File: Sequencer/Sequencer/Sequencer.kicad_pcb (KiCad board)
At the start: 2 copper layers, 163 x 116.5 mm, 158 parts, among them J1 Conn_02x05_Odd_Even, J10 Conn_01x08, J11 Conn_01x08, J12 Conn_01x08, J2 Conn_01x08, J3 Conn_01x08, J4 Conn_01x03, J5 Conn_01x04, J6 Conn_01x05, J7 Conn_01x04, J8 Conn_01x08, J9 Conn_01x08, Q1 2N3904, U1 4013, U10 TL074, U11 TL072, U12 LM285Z-ADJ, U2 40106, U3 40106, U4 40193, U5 40106, U6 4514, U7 TL072, U8 CD4094, U9 CD74HC4067M

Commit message: Sequencer - minor progress on routing
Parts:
- C1, C11, C12, C13, C14, C15, C16, C17, C2, C20, C21, C22, C23, C24, C25, C26, C27, C3, C4, C5, C6, C7, C8, C9: footprint Capacitor_THT:C_Disc_D3.0mm_W1.6mm_P2.50mm -> Capacitor_THT:C_Disc_D5.0mm_W2.5mm_P2.50mm
- R1, R10, R11, R12, R13, R14, R15, R16, R17, R18, R19, R2, R20, R21, R22, R23, R24, R25, R26, R27, R28, R29, R3, R30, R31, R32, R33, R34, R35, R36, R37, R38, R39, R4, R40, R41, R42, R43, R44, R45, R46, R47, R48, R49, R5, R50, R51, R52, R53, R54, R55, R56, R57, R58, R59, R6, R60, R61, R62, R63, R64, R65, R66, R67, R68, R69, R7, R70, R71, R72, R73, R74, R75, R76, R77, R78, R79, R8, R80, R81, R82, R83, R84, R85, R86, R87, R9: footprint Resistor_THT:R_Axial_DIN0207_L6.3mm_D2.5mm_P7.62mm_Horizontal -> Library:R_Axial_DIN0207_L6.3mm_D2.5mm_P7.62mm_Horizontal
- U6, U9: footprint Package_SO:SOIC-24W_7.5x15.4mm_P1.27mm -> Package_DIP:DIP-24_W15.24mm_Socket_LongPads
- moved R50 294.4 mm to (4.57, 29.5), turned to 90 degrees
- moved R49 290.4 mm to (7.11, 29.5), turned to 90 degrees
- moved R56 271.9 mm to (26.4, 21.6), turned to 90 degrees
- moved R48 269.2 mm to (9.65, 21.6), turned to 90 degrees
- moved R52 268.4 mm to (14.7, 21.6), turned to 90 degrees
- moved R55 267.7 mm to (29.0, 21.6), turned to 90 degrees
- moved R47 265.4 mm to (12.2, 21.6), turned to 90 degrees
- moved R51 264.5 mm to (17.3, 21.6), turned to 90 degrees
- moved R58 260.8 mm to (31.5, 21.6), turned to 90 degrees
- moved R62 260.0 mm to (41.7, 21.6), turned to 90 degrees
- moved R57 256.9 mm to (34.0, 21.6), turned to 90 degrees
- moved R54 256.1 mm to (19.8, 21.6), turned to 90 degrees
- moved R61 255.9 mm to (44.2, 21.6), turned to 90 degrees
- moved R53 252.4 mm to (22.4, 21.6), turned to 90 degrees
- moved C27 247.4 mm to (17.8, 34.5), turned to 180 degrees
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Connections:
- C1 pad 1: STRN -> Net-(C1-Pad1)
- C26 pad 2: Net-(U10C-+) -> PORT_3
- C3 pad 1: STRN -> Net-(C1-Pad1)
- D14 pad 1: GND -> DN
- D15 pad 1: GND -> UP
- J2 pad 1: S1 -> FWD
- J6 pad 2: unconnected-(J6-Pin_2-Pad2) -> CLKOUT
- R1 pad 1: STRN -> Net-(C1-Pad1)
- R1 pad 2: Net-(R1-Pad2) -> STRN
- R3 pad 2: STRN -> Net-(C1-Pad1)
- R41 pad 1: unconnected-(R41-Pad1) -> Net-(R41-Pad1)
- R42 pad 2: Net-(R42-Pad2) -> Net-(R41-Pad1)
- R43 pad 2: Net-(R42-Pad2) -> Net-(R41-Pad1)
- R47 pad 1: F2 -> FR2
- R48 pad 1: F2 -> FR2
- R49 pad 1: F1 -> FR1
- R50 pad 1: F1 -> FR1
- R51 pad 1: F3 -> FR3
- R52 pad 1: F3 -> FR3
- R53 pad 1: F4 -> FR4
- R54 pad 1: F4 -> FR4
- R55 pad 1: F5 -> FR5
- R56 pad 1: F5 -> FR5
- R57 pad 1: F6 -> FR6
- R58 pad 1: F6 -> FR6
- R59 pad 1: F7 -> FR7
- R60 pad 1: F7 -> FR7
- R61 pad 1: F8 -> FR8
- R62 pad 1: F8 -> FR8
- R63 pad 1: F9 -> FR9
- R64 pad 1: F9 -> FR9
- R65 pad 1: F10 -> FR10
- R66 pad 1: F10 -> FR10
- R67 pad 1: F11 -> FR11
- R68 pad 1: F11 -> FR11
- R69 pad 1: F12 -> FR12
- R70 pad 1: F12 -> FR12
- R71 pad 1: F13 -> FR13
- R72 pad 1: F13 -> FR13
- R73 pad 1: F14 -> FR14
- R74 pad 1: F14 -> FR14
- R75 pad 1: F15 -> FR15
- R76 pad 1: F15 -> FR15
- R77 pad 1: F16 -> FR16
- R78 pad 1: F16 -> FR16
- R86 pad 1: Net-(U10B-+) -> PORT_1_2
- U10 pad 10: Net-(U10C-+) -> PORT_3
- U10 pad 12: Net-(U10B-+) -> PORT_1_2
- U10 pad 5: Net-(U10B-+) -> PORT_1_2
- U6 pad 11: S1 -> FWD
- U7 pad 1: Net-(R42-Pad2) -> Net-(R41-Pad1)
- U9 pad 16: F1 -> FR16
- U9 pad 17: F1 -> FR15
- U9 pad 18: F1 -> FR14
- U9 pad 19: F1 -> FR13
- U9 pad 2: F1 -> FR8
- U9 pad 20: F1 -> FR12
- U9 pad 21: F1 -> FR11
- U9 pad 22: F1 -> FR10
- U9 pad 23: F1 -> FR9
- U9 pad 3: F1 -> FR7
- U9 pad 4: F1 -> FR6
- U9 pad 5: F1 -> FR5
- U9 pad 6: F1 -> FR4
- U9 pad 7: F1 -> FR3
- U9 pad 8: F1 -> FR2
- U9 pad 9: F1 -> FR1
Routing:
- net FR16: track 0.00 -> 53.2 mm
- net FR1: track 0.00 -> 51.5 mm
- net FR15: track 0.00 -> 46.2 mm
- net FR2: track 0.00 -> 46.1 mm
- net FR14: track 0.00 -> 39.6 mm
- net FR3: track 0.00 -> 38.8 mm
- net Net-(R41-Pad1): track 0.00 -> 35.6 mm
- net FR13: track 0.00 -> 32.0 mm
- net FR4: track 0.00 -> 31.8 mm
- net FR12: track 0.00 -> 23.2 mm
- net FR5: track 0.00 -> 23.0 mm
- net Net-(C27-Pad1): track 0.00 -> 18.3 mm
- net Net-(D5-A): track 0.00 -> 17.0 mm
- net Net-(C5-Pad1): track 0.00 -> 16.4 mm
- net Net-(C4-Pad1): track 0.00 -> 16.4 mm
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- added copper zone on In2.Cu, net +12V
- added copper zone on B.Cu, net -12V
- added copper zone on In1.Cu, net GND
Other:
- copper layers 2 -> 4

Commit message: Sequencer - mostly positionned
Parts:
- moved C12 203.4 mm to (33.0, 77.7), turned to -90 degrees
- moved C11 197.3 mm to (39.9, 77.7), turned to 180 degrees
- moved R31 172.7 mm to (22.1, 77.7)
- moved R30 165.3 mm to (29.7, 75.2), turned to 180 degrees
- moved R29 163.3 mm to (32.3, 75.2)
- moved D11 153.2 mm to (64.5, 82.8)
- moved C19 147.0 mm to (44.6, 112.3), turned to 180 degrees
- moved C14 140.9 mm to (79.5, 30.0), turned to -90 degrees
- moved C15 139.2 mm to (74.4, 30.0), turned to -90 degrees
- moved R46 137.9 mm to (69.3, 30.0), turned to -90 degrees
- moved C18 137.7 mm to (54.1, 96.5), turned to 90 degrees
- moved R36 133.4 mm to (79.5, 35.6), turned to -90 degrees
- moved R37 131.6 mm to (74.4, 35.6), turned to -90 degrees
- moved R34 130.8 mm to (71.9, 35.6), turned to -90 degrees
- moved C4 129.0 mm to (148.4, 43.6), turned to 180 degrees
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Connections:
- J7 pad 4: RATE_3 -> CLK
- R24 pad 2: Net-(R24-Pad2) -> RATE_1_2
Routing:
- net Net-(C11-Pad2): track 0.00 -> 10.2 mm
- net Net-(C11-Pad1): track 0.00 -> 5.59 mm
- net Net-(D12-K): track 0.00 -> 5.59 mm
- net Net-(D7-A): track 0.00 -> 3.05 mm
- net Net-(D6-A): track 0.00 -> 3.05 mm
- net RND: track 0.00 -> 3.05 mm

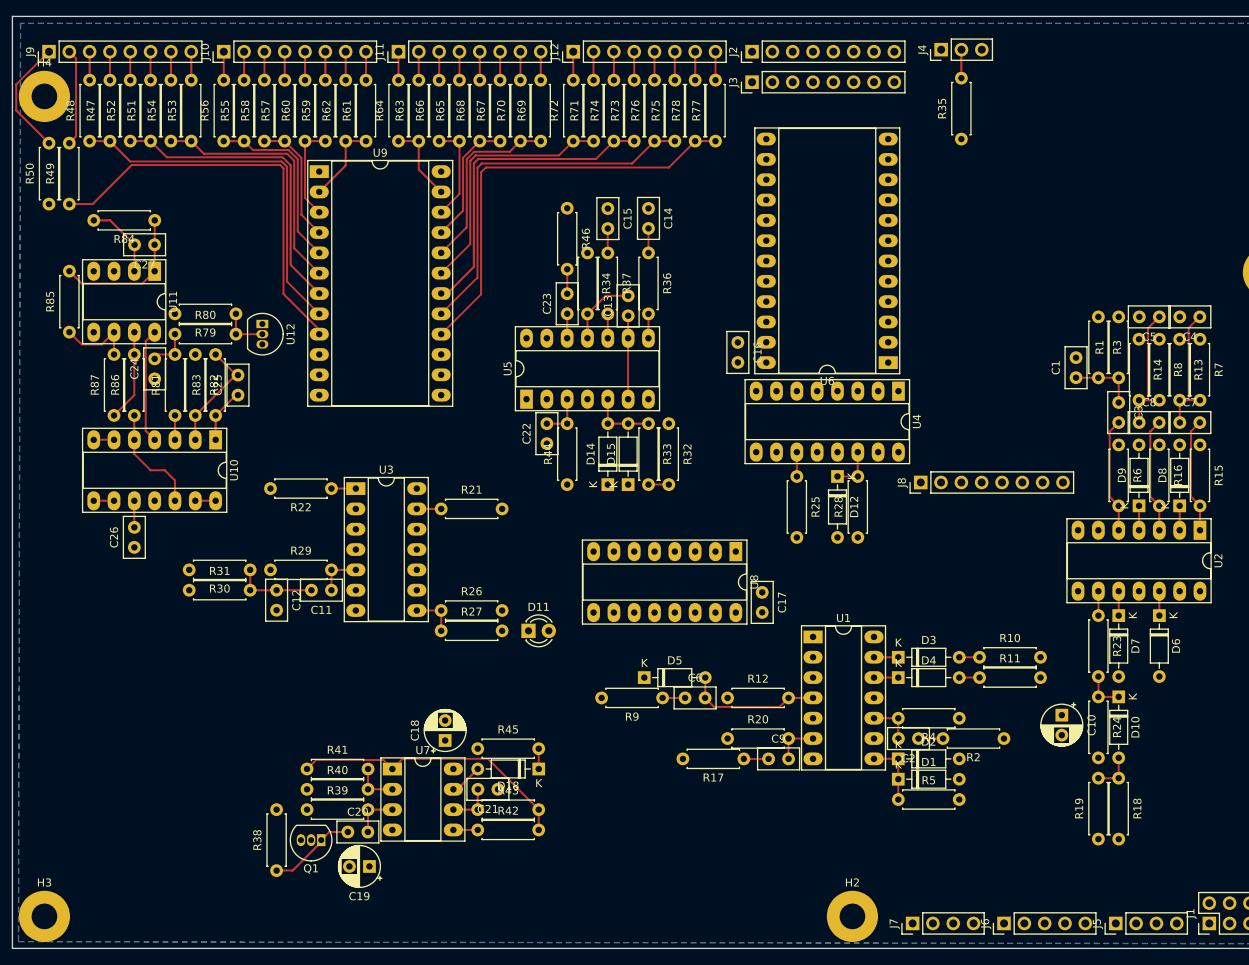
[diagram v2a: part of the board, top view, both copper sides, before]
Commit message: Sequencer - autorouted
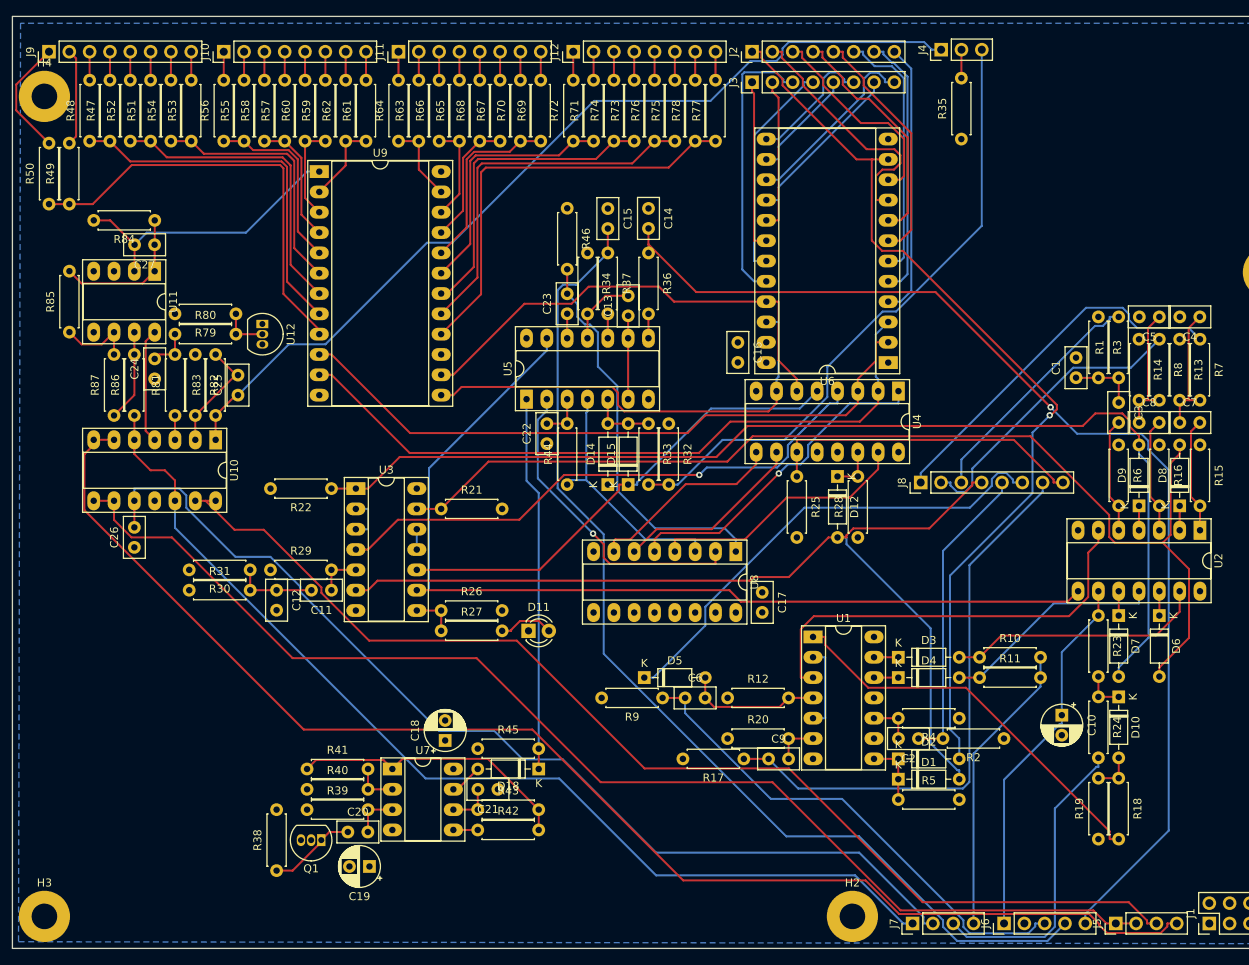
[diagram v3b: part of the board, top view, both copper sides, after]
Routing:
- net CLK: track 0.00 -> 169.9 mm
- net CV3: track 2.54 -> 171.3 mm
- net CV1: track 2.54 -> 153.6 mm
- net CV2: track 2.54 -> 143.9 mm
- net GATE: track 3.07 -> 141.4 mm, vias 0 -> 1
- net Net-(D7-A): track 3.05 -> 138.5 mm
- net Net-(D6-A): track 3.05 -> 136.9 mm
- net TRIG: track 3.05 -> 133.0 mm
- net PORT_3: track 3.32 -> 128.9 mm
- net RST: track 0.00 -> 121.5 mm
- net PORT_1_2: track 13.8 -> 129.9 mm
- net FWD: track 0.00 -> 115.6 mm, vias 0 -> 1
- net VSRC: track 6.89 -> 113.9 mm
- net QB: track 0.00 -> 87.4 mm
- net QA: track 0.00 -> 83.0 mm
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
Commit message: Sequencer - misc
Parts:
- removed D11: LED, LED_THT:LED_D3.0mm
- added J13: Conn_01x04, Connector_PinHeader_2.54mm:PinHeader_1x01_P2.54mm_Vertical, F.Cu at (125.0, 34.0)
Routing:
- net RIN: track 6.92 -> 100.4 mm, vias 0 -> 3
